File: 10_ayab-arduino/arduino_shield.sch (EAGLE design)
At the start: 19 parts, among them IC3 PCF8574T, IC4 PCF8574T

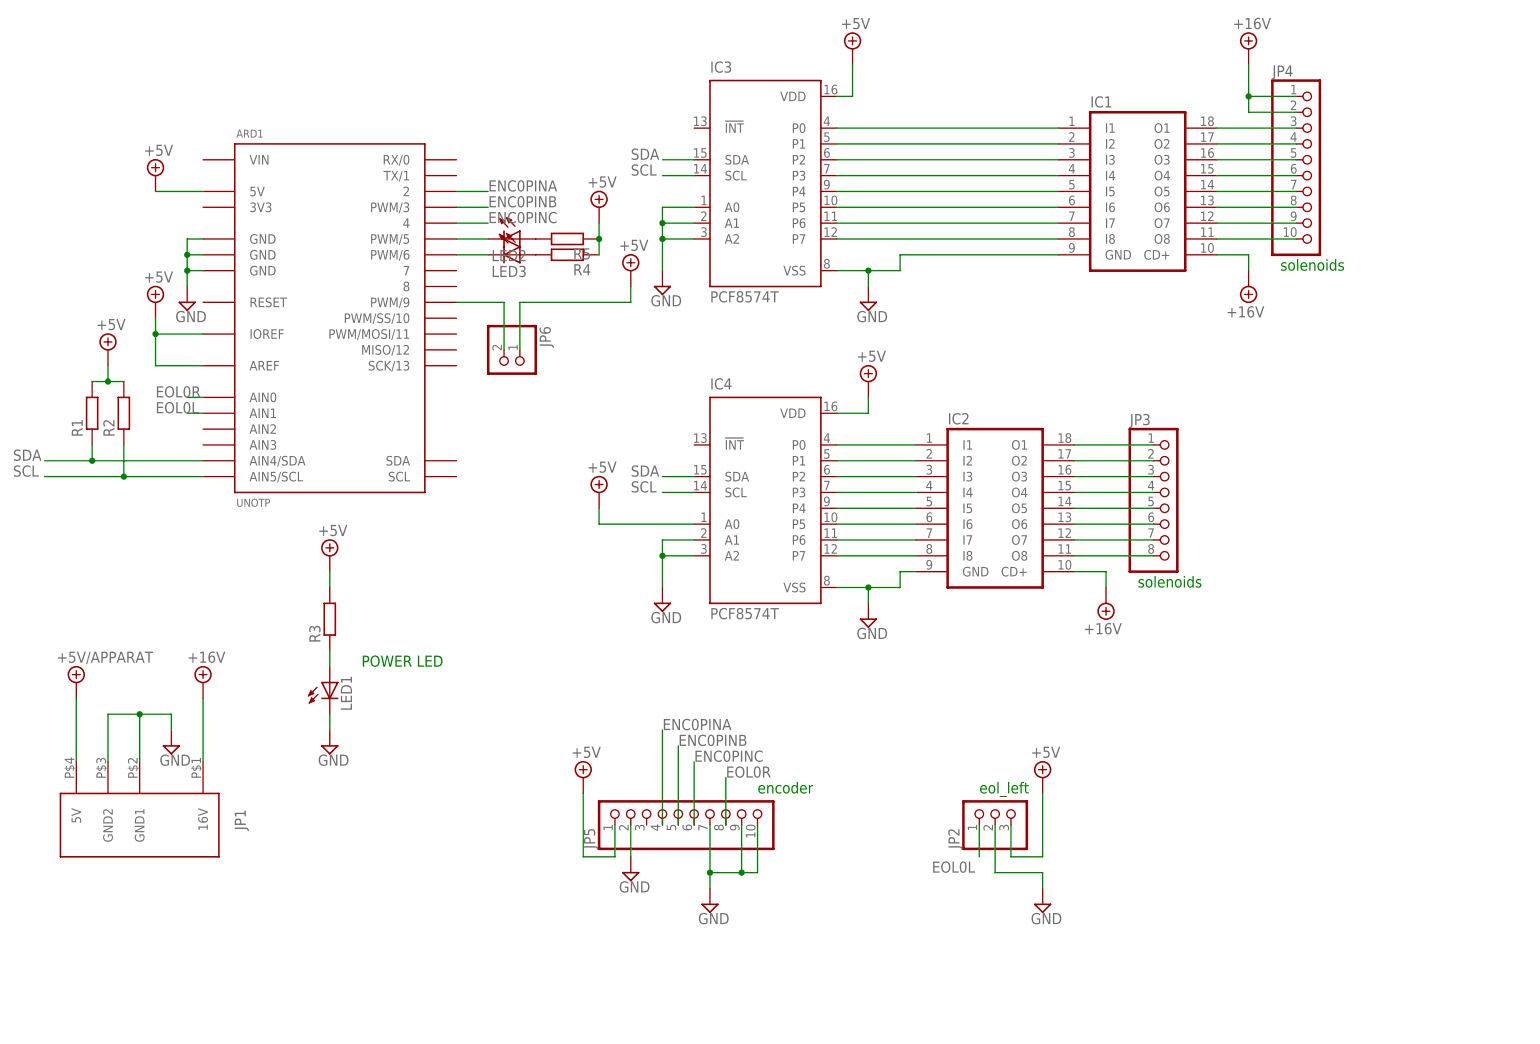
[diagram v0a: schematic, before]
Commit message: started work on improving shield, added reset button to schematic
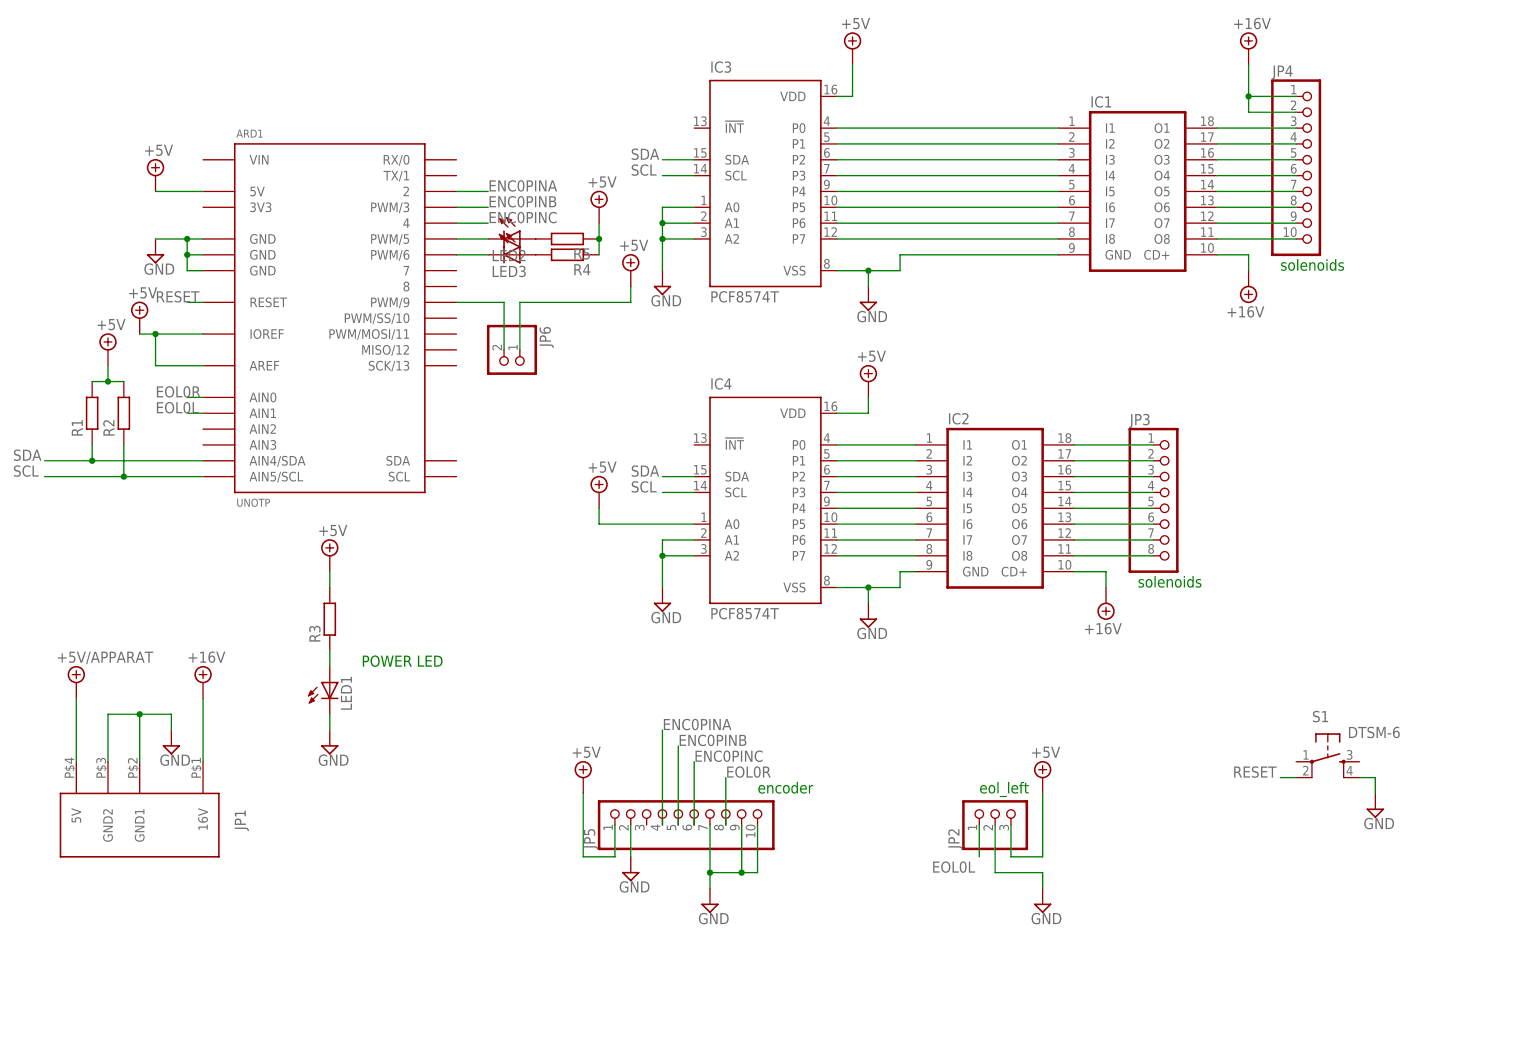
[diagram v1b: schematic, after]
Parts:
- added S1: DTSM-6, switch-tact:DTSM-6
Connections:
- new net RESET: ARD1.RESET, S1.2
- net GND: now also S1.4
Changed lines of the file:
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@@
 <part name="FRAME1" library="frames" deviceset="A4L-LOC" device=""/>
 <part name="JP6" library="pinhead" deviceset="PINHD-1X2" device=""/>
+<part name="S1" library="switch-tact" deviceset="DTSM-6" device=""/>
+<part name="SUPPLY27" library="supply2" deviceset="GND" device=""/>
 </parts>
 <sheets>
@@
 <instance part="SUPPLY13" gate="+15V" x="-99.06" y="-33.02"/>
 <instance part="SUPPLY14" gate="GND" x="-104.14" y="-43.18"/>
-<instance part="SUPPLY2" gate="GND" x="-101.6" y="27.94"/>
+<instance part="SUPPLY2" gate="GND" x="-106.68" y="35.56"/>
 <instance part="SUPPLY4" gate="GND" x="-25.4" y="30.48"/>
 <instance part="SUPPLY8" gate="GND" x="-25.4" y="-20.32"/>
@@
 <instance part="SUPPLY12" gate="GND" x="-30.48" y="-63.5"/>
 <instance part="SUPPLY19" gate="GND" x="-17.78" y="-68.58"/>
-<instance part="SUPPLY20" gate="+5V" x="-106.68" y="27.94"/>
+<instance part="SUPPLY20" gate="+5V" x="-109.22" y="25.4"/>
 <instance part="SUPPLY15" gate="G$1" x="-119.38" y="-33.02"/>
 <instance part="SUPPLY22" gate="+5V" x="-78.74" y="-12.7"/>
@@
 <instance part="FRAME1" gate="G$1" x="-142.24" y="-96.52"/>
 <instance part="JP6" gate="G$1" x="-50.8" y="17.78" rot="R270"/>
+<instance part="S1" gate="G$1" x="81.28" y="-45.72" rot="R270"/>
+<instance part="SUPPLY27" gate="GND" x="88.9" y="-53.34"/>
 </instances>
 <busses>
@@
 <pinref part="SUPPLY20" gate="+5V" pin="+5V"/>
 <wire x1="-99.06" y1="22.86" x2="-106.68" y2="22.86" width="0.1524" layer="91"/>
-<wire x1="-106.68" y1="22.86" x2="-106.68" y2="25.4" width="0.1524" layer="91"/>
+<wire x1="-106.68" y1="22.86" x2="-109.22" y2="22.86" width="0.1524" layer="91"/>
 <pinref part="ARD1" gate="G$1" pin="AREF"/>
 <wire x1="-99.06" y1="17.78" x2="-106.68" y2="17.78" width="0.1524" layer="91"/>
@@
 </net>
 <net name="GND" class="0">
-<segment>
-<pinref part="ARD1" gate="G$1" pin="GND@3"/>
-<wire x1="-99.06" y1="33.02" x2="-101.6" y2="33.02" width="0.1524" layer="91"/>
-<wire x1="-101.6" y1="33.02" x2="-101.6" y2="30.48" width="0.1524" layer="91"/>
-<pinref part="SUPPLY2" gate="GND" pin="GND"/>
-<pinref part="ARD1" gate="G$1" pin="GND@1"/>
-<wire x1="-99.06" y1="38.1" x2="-101.6" y2="38.1" width="0.1524" layer="91"/>
-<wire x1="-101.6" y1="38.1" x2="-101.6" y2="35.56" width="0.1524" layer="91"/>
-<junction x="-101.6" y="33.02"/>
-<pinref part="ARD1" gate="G$1" pin="GND@2"/>
-<wire x1="-101.6" y1="35.56" x2="-101.6" y2="33.02" width="0.1524" layer="91"/>
-<wire x1="-99.06" y1="35.56" x2="-101.6" y2="35.56" width="0.1524" layer="91"/>
-<junction x="-101.6" y="35.56"/>
-</segment>
 <segment>
 <pinref part="IC3" gate="G$1" pin="A0"/>
@@
 <junction x="-109.22" y="-38.1"/>
 </segment>
+<segment>
+<pinref part="ARD1" gate="G$1" pin="GND@3"/>
+<wire x1="-99.06" y1="33.02" x2="-101.6" y2="33.02" width="0.1524" layer="91"/>
+<pinref part="ARD1" gate="G$1" pin="GND@1"/>
+<wire x1="-99.06" y1="38.1" x2="-101.6" y2="38.1" width="0.1524" layer="91"/>
+<wire x1="-101.6" y1="38.1" x2="-101.6" y2="35.56" width="0.1524" layer="91"/>
+<pinref part="ARD1" gate="G$1" pin="GND@2"/>
+<wire x1="-101.6" y1="35.56" x2="-101.6" y2="33.02" width="0.1524" layer="91"/>
+<wire x1="-99.06" y1="35.56" x2="-101.6" y2="35.56" width="0.1524" layer="91"/>
+<junction x="-101.6" y="35.56"/>
+<pinref part="SUPPLY2" gate="GND" pin="GND"/>
+<wire x1="-106.68" y1="38.1" x2="-101.6" y2="38.1" width="0.1524" layer="91"/>
+<junction x="-101.6" y="38.1"/>
+</segment>
+<segment>
+<pinref part="S1" gate="G$1" pin="4"/>
+<pinref part="SUPPLY27" gate="GND" pin="GND"/>
+<wire x1="86.36" y1="-48.26" x2="88.9" y2="-48.26" width="0.1524" layer="91"/>
+<wire x1="88.9" y1="-48.26" x2="88.9" y2="-50.8" width="0.1524" layer="91"/>
+</segment>
 </net>
 <net name="+15V" class="0">
@@
 </segment>
 </net>
+<net name="RESET" class="0">
+<segment>
+<pinref part="ARD1" gate="G$1" pin="RESET"/>
+<wire x1="-99.06" y1="27.94" x2="-101.6" y2="27.94" width="0.1524" layer="91"/>
+<label x="-106.68" y="27.94" size="1.778" layer="95"/>
+</segment>
+<segment>
+<pinref part="S1" gate="G$1" pin="2"/>
+<wire x1="76.2" y1="-48.26" x2="73.66" y2="-48.26" width="0.1524" layer="91"/>
+<label x="66.04" y="-48.26" size="1.778" layer="95"/>
+</segment>
+</net>

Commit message: added kh-930 specific connectors
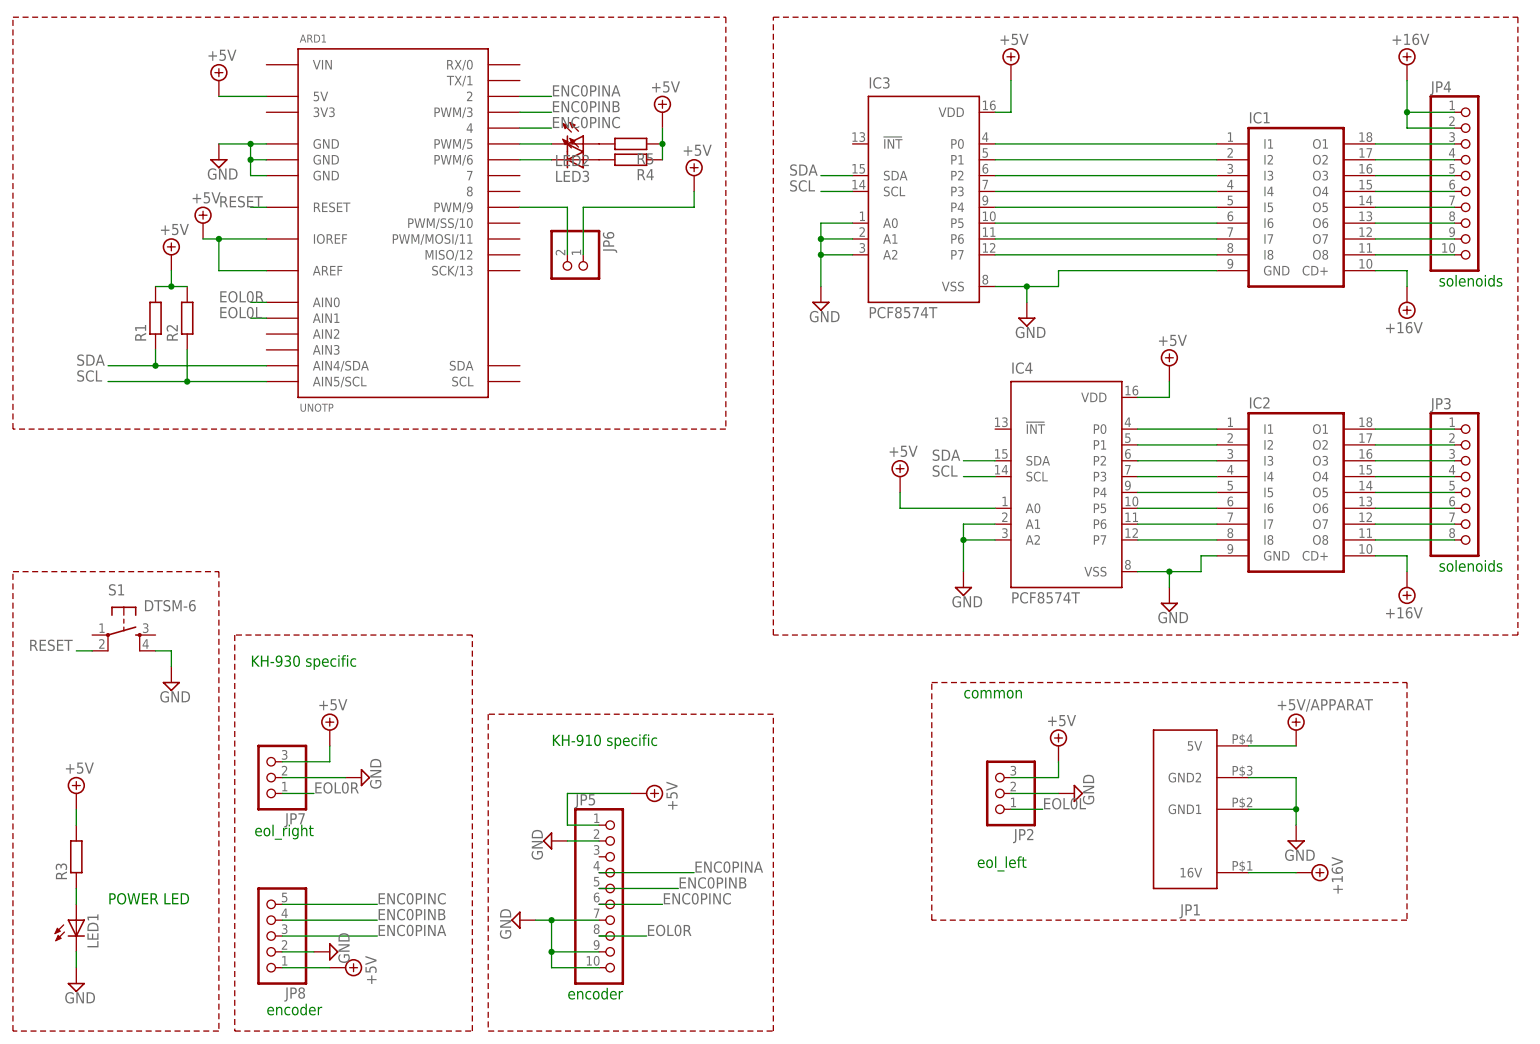
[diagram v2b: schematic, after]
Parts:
- added JP7: (no value), pinheader_250:PINHD-1X3
- added JP8: (no value), pinheader_250:PINHD-1X5
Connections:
- net +5V: now also JP7.3, JP8.1
- net ENC0PINA: now also JP8.3
- net ENC0PINB: now also JP8.4
- net ENC0PINC: now also JP8.5
- net EOL0R: now also JP7.1
- net GND: now also JP7.2, JP8.2
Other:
- note added: "KH-910 specific"
- note added: "KH-930 specific"
- note added: "common"
- note added: "eol_right"
- moved on the sheet: ARD1, IC1, IC2, IC3, IC4, JP1, JP2, JP3, JP4, JP5, JP6, LED1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

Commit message: added gerber data for ayab-shield-v1.1 added kh-930 manual
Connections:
- new net DFG: ARD1.2
- new net QEWRT: ARD1.PWM/3
- net ENC0PINA: no longer ARD1.2
- net ENC0PINB: no longer ARD1.PWM/3
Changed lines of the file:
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@@
 </segment>
 </net>
-<net name="ENC0PINA" class="0">
+<net name="DFG" class="0">
 <segment>
 <pinref part="ARD1" gate="G$1" pin="2"/>
@@
 <label x="-43.18" y="60.96" size="1.778" layer="95"/>
 </segment>
-<segment>
-<pinref part="JP5" gate="A" pin="4"/>
-<wire x1="-35.56" y1="-63.5" x2="-20.32" y2="-63.5" width="0.1524" layer="91"/>
-<label x="-20.32" y="-63.5" size="1.778" layer="95"/>
-</segment>
-<segment>
-<pinref part="JP8" gate="A" pin="3"/>
-<wire x1="-86.36" y1="-73.66" x2="-71.12" y2="-73.66" width="0.1524" layer="91"/>
-<label x="-71.12" y="-73.66" size="1.778" layer="95"/>
-</segment>
-</net>
-<net name="ENC0PINB" class="0">
+</net>
+<net name="QEWRT" class="0">
 <segment>
 <pinref part="ARD1" gate="G$1" pin="PWM/3"/>
 <wire x1="-48.26" y1="58.42" x2="-43.18" y2="58.42" width="0.1524" layer="91"/>
 <label x="-43.18" y="58.42" size="1.778" layer="95"/>
-</segment>
-<segment>
-<pinref part="JP5" gate="A" pin="5"/>
-<wire x1="-35.56" y1="-66.04" x2="-22.86" y2="-66.04" width="0.1524" layer="91"/>
-<label x="-22.86" y="-66.04" size="1.778" layer="95"/>
-</segment>
-<segment>
-<pinref part="JP8" gate="A" pin="4"/>
-<wire x1="-86.36" y1="-71.12" x2="-71.12" y2="-71.12" width="0.1524" layer="91"/>
-<label x="-71.12" y="-71.12" size="1.778" layer="95"/>
 </segment>
 </net>
@@
 </segment>
 </net>
+<net name="ENC0PINA" class="0">
+<segment>
+<pinref part="JP5" gate="A" pin="4"/>
+<wire x1="-35.56" y1="-63.5" x2="-20.32" y2="-63.5" width="0.1524" layer="91"/>
+<label x="-20.32" y="-63.5" size="1.778" layer="95"/>
+</segment>
+<segment>
+<pinref part="JP8" gate="A" pin="3"/>
+<wire x1="-86.36" y1="-73.66" x2="-71.12" y2="-73.66" width="0.1524" layer="91"/>
+<label x="-71.12" y="-73.66" size="1.778" layer="95"/>
+</segment>
+</net>
+<net name="ENC0PINB" class="0">
+<segment>
+<pinref part="JP5" gate="A" pin="5"/>
+<wire x1="-35.56" y1="-66.04" x2="-22.86" y2="-66.04" width="0.1524" layer="91"/>
+<label x="-22.86" y="-66.04" size="1.778" layer="95"/>
+</segment>
+<segment>
+<pinref part="JP8" gate="A" pin="4"/>
+<wire x1="-86.36" y1="-71.12" x2="-71.12" y2="-71.12" width="0.1524" layer="91"/>
+<label x="-71.12" y="-71.12" size="1.778" layer="95"/>
+</segment>
+</net>
